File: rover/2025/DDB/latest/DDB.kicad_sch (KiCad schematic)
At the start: 93 parts, among them J1 USB_C_USB4105-GF-A, J2 ETH-RJHSE508104, J3 TerminalBlock, J4 ETH-RJHSE508104, J8 XT30PW-F, SW1 TS09-63-25-WT-160-SMT-TR, SW2 TS09-63-25-WT-160-SMT-TR, U1 ESP32-S3-WROVER, U10 HSS-VN7140ASTR, U11 HSS-VN7140ASTR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

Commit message: Multiple changes to lib + added + fixed pins ERC checks
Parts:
- C10, C9: value C -> 10uF
- C8: value C -> 100nF
- D1, D2: value LED -> R
- D3: value LED -> G
- D4, D5: value LED -> B
- F1: value FuseHolder -> 20A
- F10, F11, F2, F3, F4, F5, F6, F7, F8: value FuseHolder -> 3A
- R11, R12, R13, R14, R15, R16, R19, R20, R27, R28, R29, R30, R31, R32, R33, R34: value R -> 15k
- R17, R18, R21, R22, R23, R24, R25, R26, R35: value R -> 5k1
- R2, R3: value k -> 5k1
- R4, R6, R7, R8: value R -> 1k
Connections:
- net +24V_L: now also F10.2, F11.2, F2.2, F3.2, F4.2, F5.2, F6.2, F7.2, F8.2; no longer F10.1, F11.1, F2.1, F3.1, F4.1, F5.1, F6.1, F7.1, F8.1
- net at U14.5 (Vcc), U14.8 (Vcc): now also F11.1; no longer F11.2
- net at U11.5 (Vcc), U11.8 (Vcc): now also F7.1; no longer F7.2
- net at U9.5 (Vcc), U9.8 (Vcc): now also F4.1; no longer F4.2
- net at U13.5 (Vcc), U13.8 (Vcc): now also F10.1; no longer F10.2
- net at J8.2 (+): now also F6.1; no longer F6.2
- net at U8.5 (Vcc), U8.8 (Vcc): now also F3.1; no longer F3.2
- net at U7.5 (Vcc), U7.8 (Vcc): now also F2.1; no longer F2.2
- net at U10.5 (Vcc), U10.8 (Vcc): now also F5.1; no longer F5.2
- net at F1.1: now also U6.8 (Vcc); no longer U5.2 (+)
- net at F1.2: now also U5.2 (+); no longer U6.8 (Vcc)
- net at U12.5 (Vcc), U12.8 (Vcc): now also F8.1; no longer F8.2
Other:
- moved on the sheet: C10, C8, C9, F1, F10, F11, F2, F3, F4, F5, F6, F7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

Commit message: .
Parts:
- removed R35: 5k1, Resistor_SMD:R_0805_2012Metric_Pad1.20x1.40mm_HandSolder, symbol Device:R
- R10, R9: value R -> 15k
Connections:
- net GND: no longer J1.S1 (SHIELD)
- no-connect marks 49 -> 50
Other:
- moved on the sheet: F1, R2, R3, U2, U5

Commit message: DDB REV 0 done
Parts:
- added R35, R36, R37, R38, R39, R40, R41, R42: 1k, Resistor_SMD:R_0805_2012Metric_Pad1.20x1.40mm_HandSolder, symbol Device:R
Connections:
- net GND: now also R35.2, R36.2, R37.2, R38.2, R39.2, R40.2, R41.2, R42.2
- net SIGN_SENSE_24_1: no longer names the net of U1.22 (IO14)
- net SIGN_SENSE_24_1: no longer U7.4 (Multisense)
- net SIGN_SENSE_24_2: no longer names the net of U1.20 (IO12)
- net SIGN_SENSE_24_2: no longer U8.4 (Multisense)
- net SIGN_SENSE_24_3: no longer names the net of U9.4 (Multisense)
- net SIGN_SENSE_24_3: now also R41.1; no longer U1.18 (IO10)
- net SIGN_SENSE_24_4: no longer names the net of U10.4 (Multisense)
- net SIGN_SENSE_24_4: now also R36.1; no longer U1.5 (IO5)
- net SIGN_SENSE_24_5: no longer names the net of U1.7 (IO7)
- net SIGN_SENSE_24_5: no longer U13.4 (Multisense)
- net SIGN_SENSE_24_6: no longer names the net of U14.4 (Multisense)
- net SIGN_SENSE_24_6: now also R42.1; no longer U1.9 (IO16)
- net SIGN_SENSE_24_7: no longer names the net of U1.11 (IO18)
- net SIGN_SENSE_24_7: no longer U11.4 (Multisense)
- net SIGN_SENSE_24_8: no longer names the net of U12.4 (Multisense)
- net SIGN_SENSE_24_8: now also R40.1; no longer U1.17 (IO9)
- new net: R37.1, U11.4 (Multisense)
- new net: R38.1, U8.4 (Multisense)
- new net: R35.1, U7.4 (Multisense)
- new net: R39.1, U13.4 (Multisense)
- no-connect marks 50 -> 58
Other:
- moved on the sheet: J3

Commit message: ARM-JL Drawing Done
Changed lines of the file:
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@@
-		)
-	)
-	(text_box "TODO: Sensing is off when SEn is pulled LOW. Either remove sign sense or pull high and figure out current sense calcs\nTODO: Add decoupling/bigger resistor to LOW_POW_EN signal (Max 7.5v)"
-		(exclude_from_sim no)
-		(at -41.91 12.7 0)
-		(size 46.99 36.83)
-		(stroke
-			(width 0)
-			(type default)
-		)
-		(fill
-			(type color)
-			(color 255 255 194 1)
-		)
-		(effects
-			(font
-				(size 1.27 1.27)
-			)
-			(justify left top)
 		)
 	)

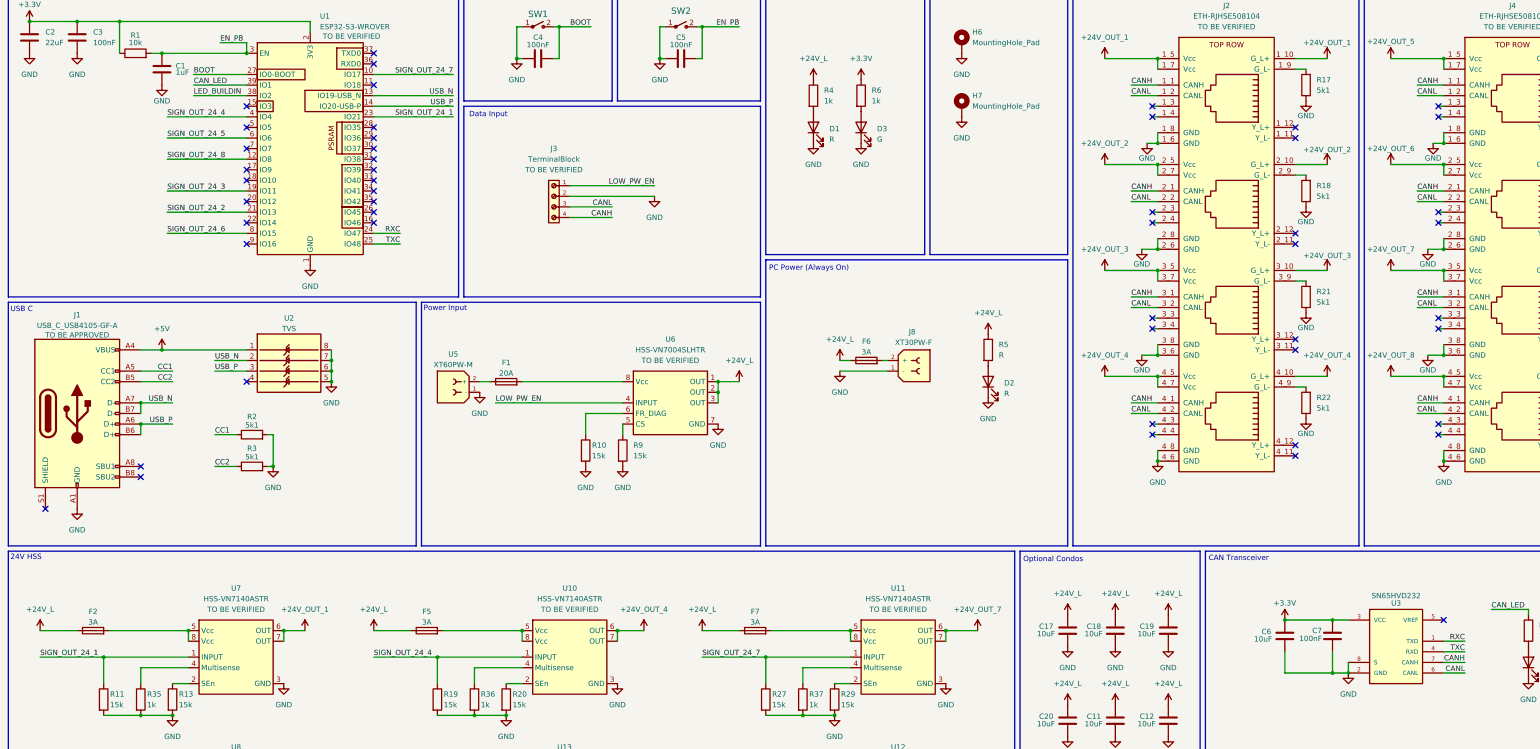
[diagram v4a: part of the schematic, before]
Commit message: Last touch before order for ARMJL, Regulator and DDB + start of J345
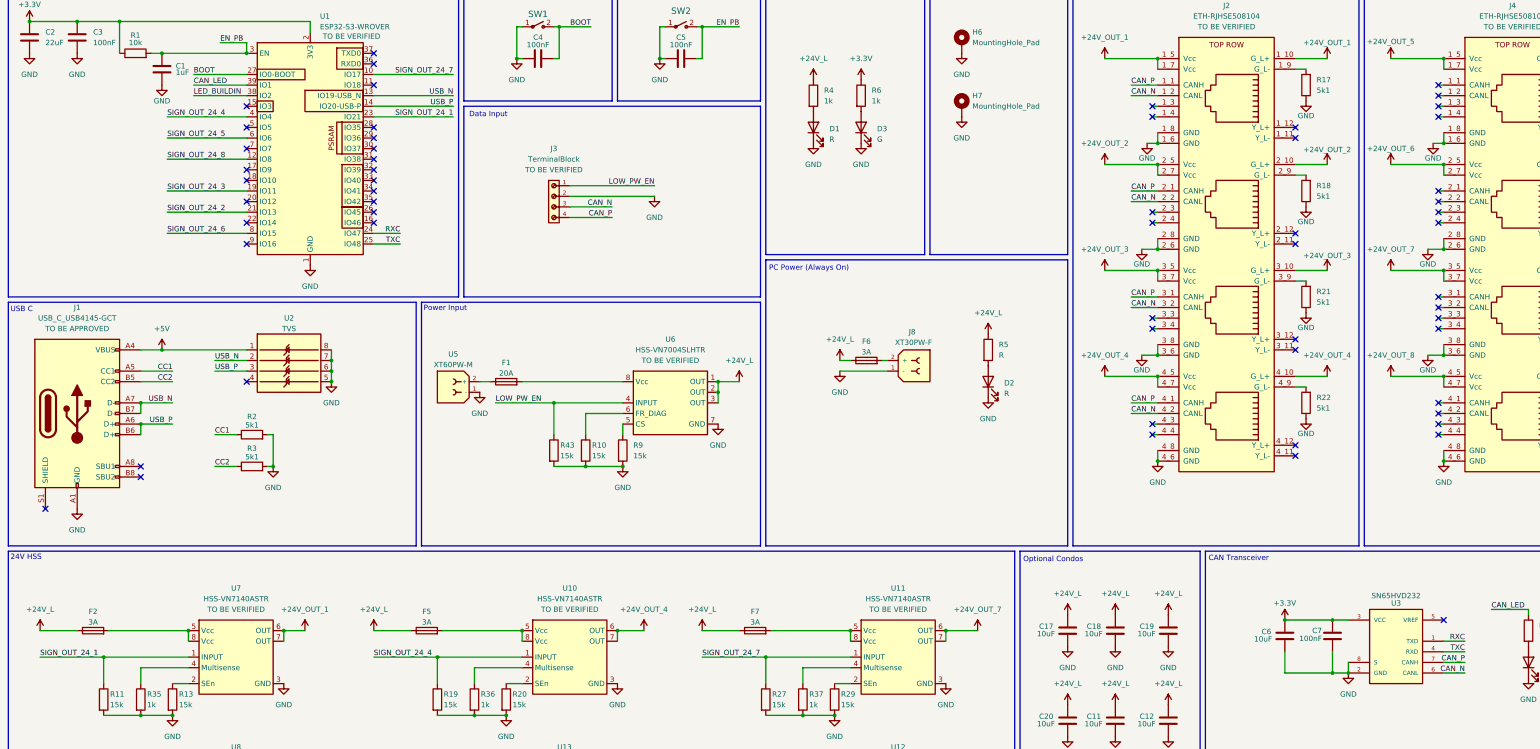
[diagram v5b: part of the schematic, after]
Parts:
- removed J1: USB_C_USB4105-GF-A, Connector_USB:USB_C_Receptacle_GCT_USB4105-xx-A_16P_TopMnt_Horizontal, symbol 0_RoverLibrary:USB_C_USB4105-GF-A
- added J1: USB_C_USB4145-GCT, RoverFootprint:USB4145_GCT, symbol 0_RoverLibrary:USB_C_USB4145-03-C
- added R43: 15k, Resistor_SMD:R_0805_2012Metric_Pad1.20x1.40mm_HandSolder, symbol Device:R
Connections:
- net +5V: now also J1.A4 (VBUS), J1.A9 (VBUS), J1.B4 (VBUS), J1.B9 (VBUS)
- net CC1: now also J1.A5 (CC1)
- net CC2: now also J1.B5 (CC2)
- net GND: now also J1.A1 (GND), J1.A12 (GND), J1.B1 (GND), J1.B12 (GND), R43.2
- net LOW_PW_EN: now also R43.1
- net USB_N: now also J1.A7 (D-), J1.B7 (D-)
- net USB_P: now also J1.A6 (D+), J1.B6 (D+)
- net CANH renamed CAN_P
- net CAN_P: no longer J4.1_1 (CANH), J4.2_1 (CANH), J4.3_1 (CANH), J4.4_1 (CANH)
- net CANL renamed CAN_N
- net CAN_N: no longer J4.1_2 (CANL), J4.2_2 (CANL), J4.3_2 (CANL), J4.4_2 (CANL)
- no-connect marks 58 -> 66

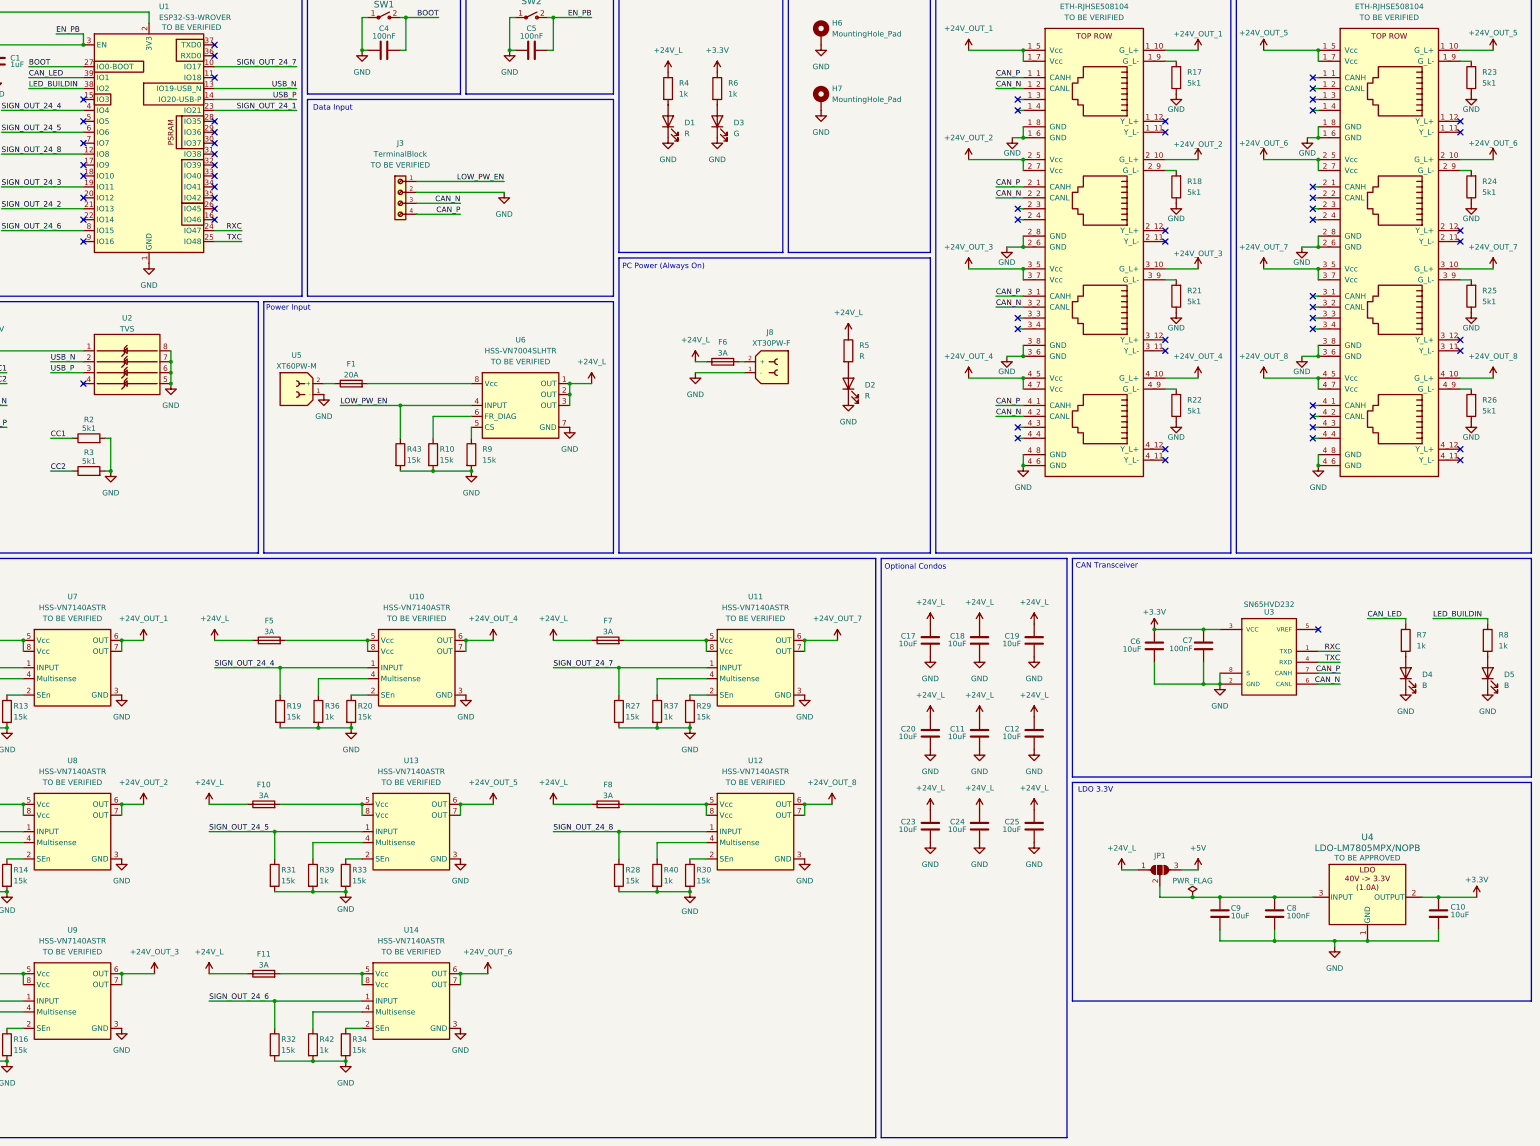
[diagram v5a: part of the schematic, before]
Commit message: Off board connections + silkscreen
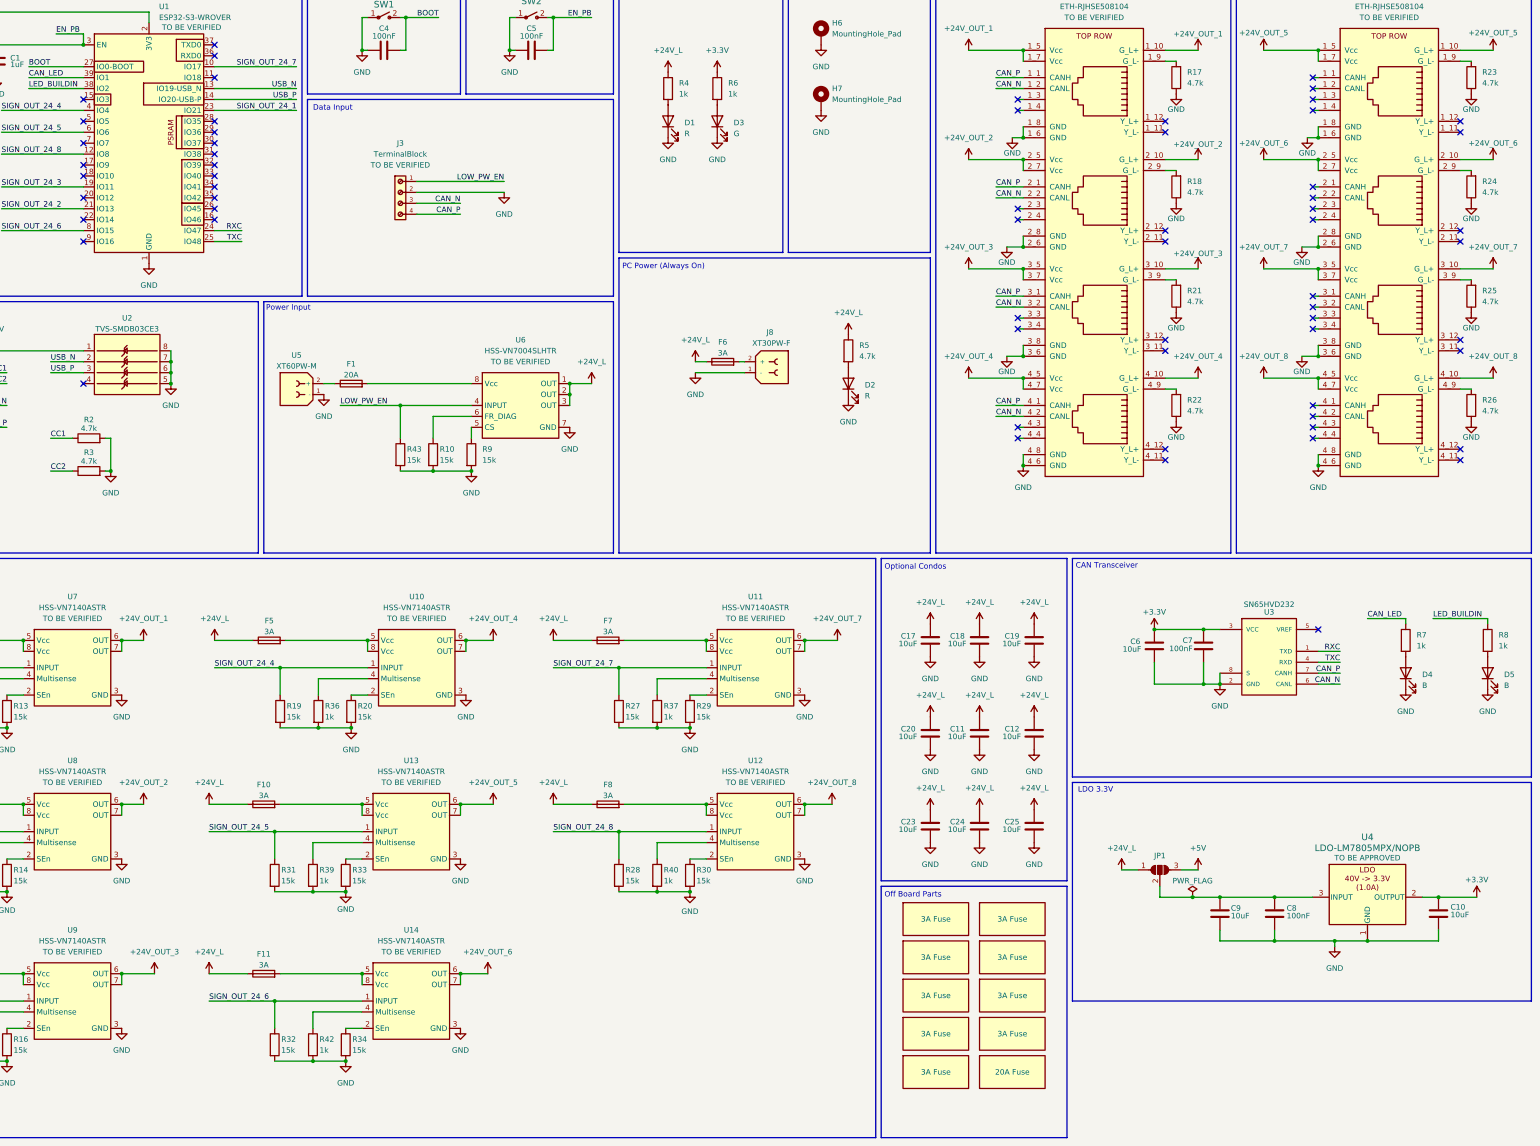
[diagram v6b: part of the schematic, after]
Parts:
- added G1, G2, G3, G4, G5, G6, G7, G8, G9: 3A Fuse, symbol 0_RoverLibrary:Off Board Part
- added G10: 20A Fuse, symbol 0_RoverLibrary:Off Board Part
- R17, R18, R2, R21, R22, R23, R24, R25, R26, R3: value 5k1 -> 4.7k
- R5: value R -> 4.7k
- U2: value TVS -> TVS-SMDB03CE3
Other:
- note added: "Off Board Parts"

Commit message: Footprint
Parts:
- U4: value LDO-LM7805MPX/NOPB -> TLE4284DV33ATMA1
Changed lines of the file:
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@@
 			)
 		)
-		(property "Value" "LDO-LM7805MPX/NOPB"
+		(property "Value" "TLE4284DV33ATMA1"
 			(at 368.3 215.9 0)
 			(effects

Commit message: Ordering pcbs
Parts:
- C10, C8, C9: footprint LED_SMD:LED_0805_2012Metric -> Capacitor_SMD:C_0805_2012Metric_Pad1.18x1.45mm_HandSolder
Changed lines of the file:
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@@
 			)
 		)
-		(property "Footprint" "LED_SMD:LED_0805_2012Metric"
+		(property "Footprint" "Capacitor_SMD:C_0805_2012Metric_Pad1.18x1.45mm_HandSolder"
 			(at 334.9752 234.95 0)
 			(effects
@@
 			)
 		)
-		(property "Footprint" "LED_SMD:LED_0805_2012Metric"
+		(property "Footprint" "Capacitor_SMD:C_0805_2012Metric_Pad1.18x1.45mm_HandSolder"
 			(at 347.6752 234.95 0)
 			(effects
@@
 			)
 		)
-		(property "Footprint" "LED_SMD:LED_0805_2012Metric"
+		(property "Footprint" "Capacitor_SMD:C_0805_2012Metric_Pad1.18x1.45mm_HandSolder"
 			(at 385.7752 234.95 0)
 			(effects
